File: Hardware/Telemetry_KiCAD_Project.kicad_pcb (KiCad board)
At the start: 4 copper layers, 80 x 93.3 mm, 68 parts, among them J1 TX SPI Debug, J2 RX SPI Debug, J3 Amphenol 132134 SMA Connector, J4 10118192-0001LF, J5 DB37_Male_MountingHoles, U1 Si4463, U2 ADL5521, U3 RSD-897.500-942.500-1612-TR, U4 LM317T, U5 USBLC6-2SC6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

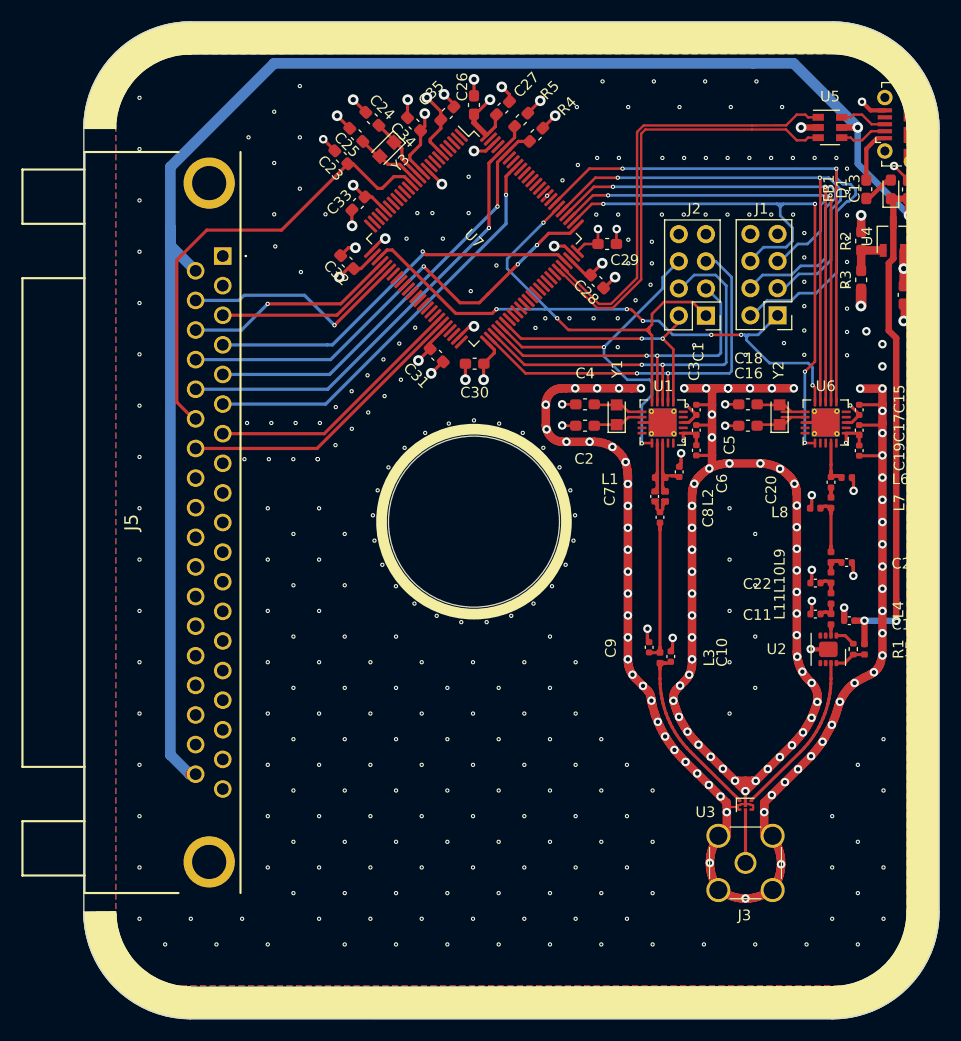
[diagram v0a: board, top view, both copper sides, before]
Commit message: Adjusted position of USB connector and components, length matched data lines
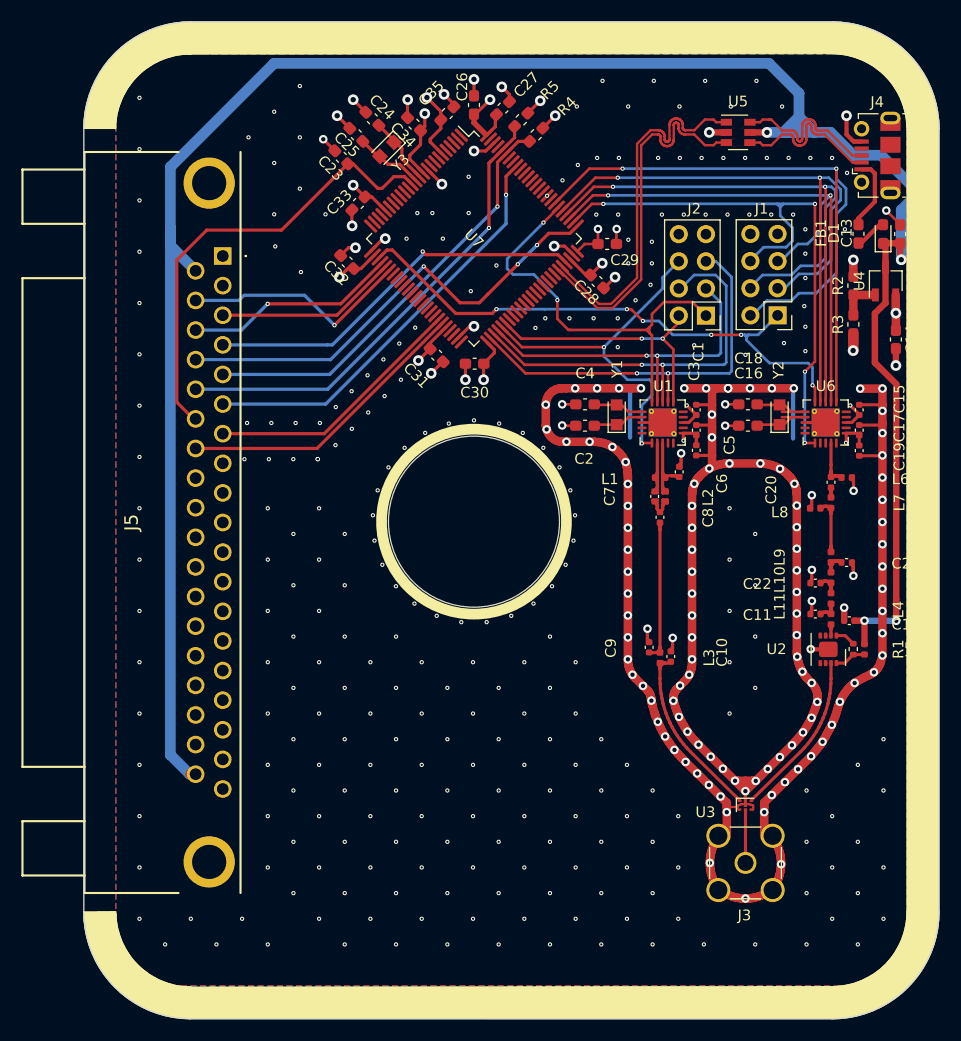
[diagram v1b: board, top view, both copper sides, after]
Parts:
- moved U5 8.60 mm to (141.2, 62.1)
- moved C14 4.23 mm to (156.0, 81.4)
- moved FB1 4.23 mm to (152.5, 71.5)
- moved C13 4.23 mm to (156.4, 71.6)
- moved D1 4.23 mm to (154.8, 71.6)
- moved R2 4.23 mm to (152.0, 76.4)
- moved R3 4.23 mm to (152.0, 80.0)
- moved U4 4.23 mm to (155.0, 76.0)
- moved J4 3.64 mm to (154.2, 64.2)
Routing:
- net +5V: track 195.6 -> 206.9 mm
- net /USB Connector and ESD/USB_CONN_D-: track 4.49 -> 15.0 mm
- net /USB Connector and ESD/USB_CONN_D+: track 4.51 -> 14.9 mm
- net GND: track 311.9 -> 322.1 mm, vias 418 -> 414
- net /USB Connector and ESD/D-: track 41.1 -> 35.0 mm
- net /USB Connector and ESD/D+: track 40.8 -> 34.7 mm
- net Net-(FB1-Pad2): track 5.07 -> 6.82 mm
- net /~RX_SEL: track 38.4 -> 39.6 mm

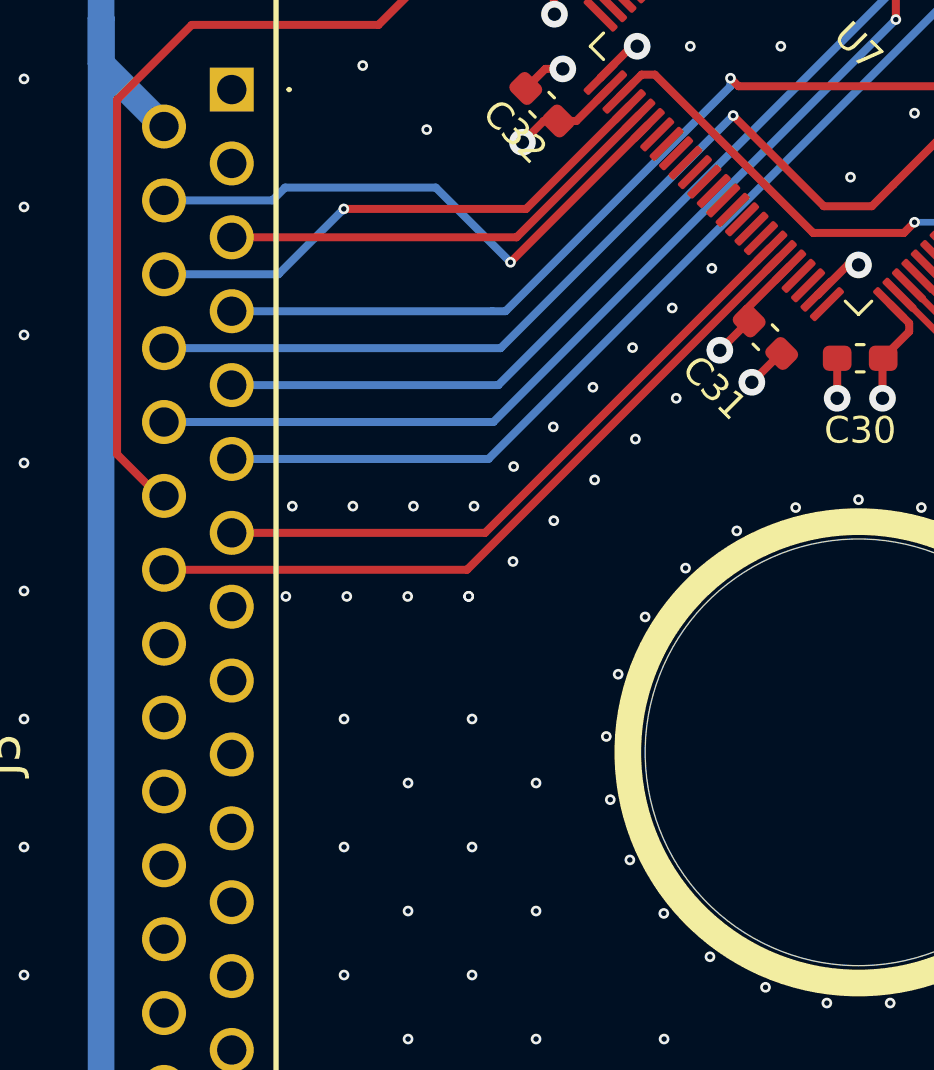
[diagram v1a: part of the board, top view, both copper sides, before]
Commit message: Added status LEDs for MCU
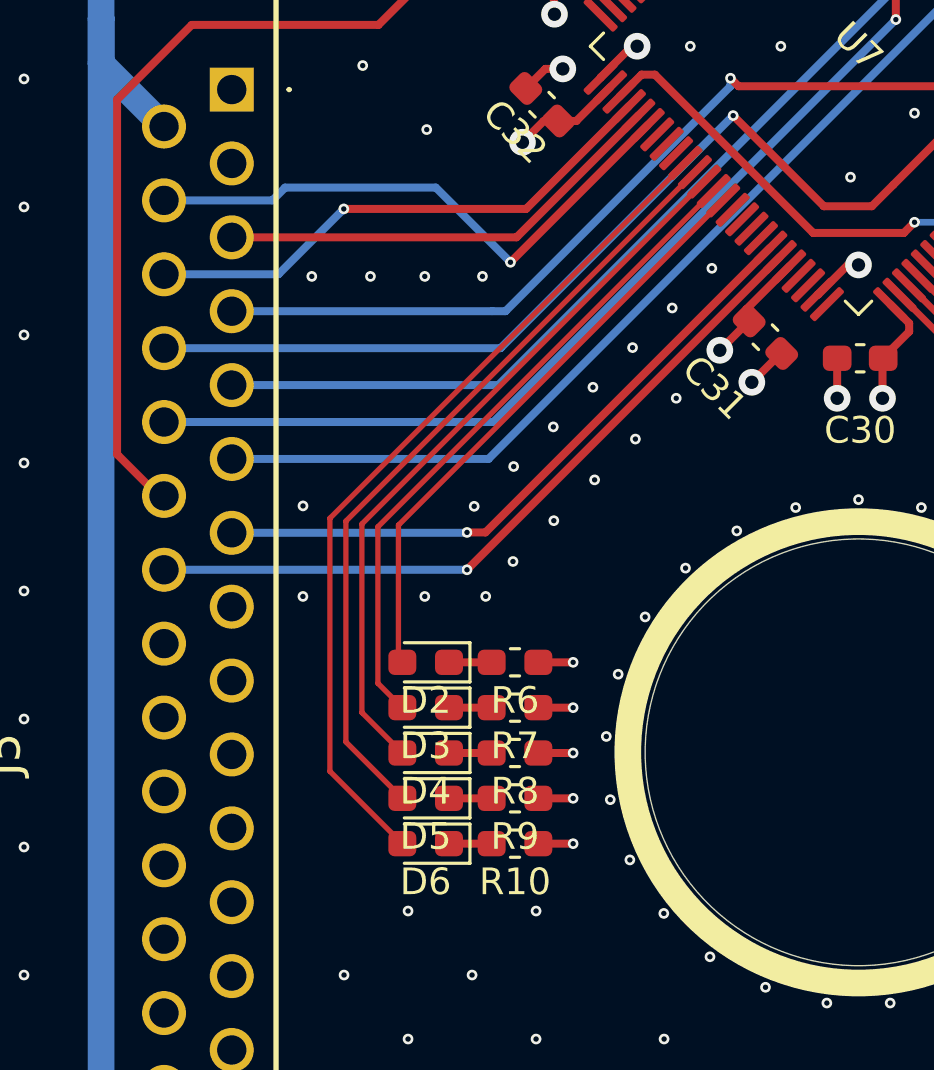
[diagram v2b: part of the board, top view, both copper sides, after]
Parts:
- added D2: Red, LED_SMD:LED_0603_1608Metric_Pad1.05x0.95mm_HandSolder, F.Cu at (100.3, 95.1)
- added D3: Grn, LED_SMD:LED_0603_1608Metric_Pad1.05x0.95mm_HandSolder, F.Cu at (100.3, 96.8)
- added D4: Red, LED_SMD:LED_0603_1608Metric_Pad1.05x0.95mm_HandSolder, F.Cu at (100.3, 98.5)
- added D5: Grn, LED_SMD:LED_0603_1608Metric_Pad1.05x0.95mm_HandSolder, F.Cu at (100.3, 100.2)
- added D6: Red, LED_SMD:LED_0603_1608Metric_Pad1.05x0.95mm_HandSolder, F.Cu at (100.3, 101.9)
- added R10: 820, Resistor_SMD:R_0603_1608Metric_Pad1.05x0.95mm_HandSolder, F.Cu at (103.6, 101.9)
- added R6: 820, Resistor_SMD:R_0603_1608Metric_Pad1.05x0.95mm_HandSolder, F.Cu at (103.6, 95.1)
- added R7: 820, Resistor_SMD:R_0603_1608Metric_Pad1.05x0.95mm_HandSolder, F.Cu at (103.6, 96.8)
- added R8: 820, Resistor_SMD:R_0603_1608Metric_Pad1.05x0.95mm_HandSolder, F.Cu at (103.6, 98.5)
- added R9: 820, Resistor_SMD:R_0603_1608Metric_Pad1.05x0.95mm_HandSolder, F.Cu at (103.6, 100.2)
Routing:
- net Net-(D6-Pad2): track 0.00 -> 32.2 mm
- net Net-(D5-Pad2): track 0.00 -> 29.8 mm
- net Net-(D4-Pad2): track 0.00 -> 27.4 mm
- net Net-(D3-Pad2): track 0.00 -> 25.0 mm
- net Net-(D2-Pad2): track 0.00 -> 22.4 mm
- net GND: track 322.1 -> 328.6 mm, vias 414 -> 413
- net Net-(D6-Pad1): track 0.00 -> 1.60 mm
- net Net-(D5-Pad1): track 0.00 -> 1.60 mm
- net Net-(D4-Pad1): track 0.00 -> 1.60 mm
- net Net-(D3-Pad1): track 0.00 -> 1.60 mm
- net Net-(D2-Pad1): track 0.00 -> 1.60 mm
- net /MCU_L562VE/ABORT_1: vias 0 -> 1
- net /MCU_L562VE/ABORT_2: vias 0 -> 1

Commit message: Added silk screen art
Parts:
- added G***: LOGO, Custom_Graphics:RDT_Logo, B.Cu at (102.7, 98.5)
- added G***: LOGO, Custom_Graphics:telemetry_qr_code, B.Cu at (121.8, 132.1)

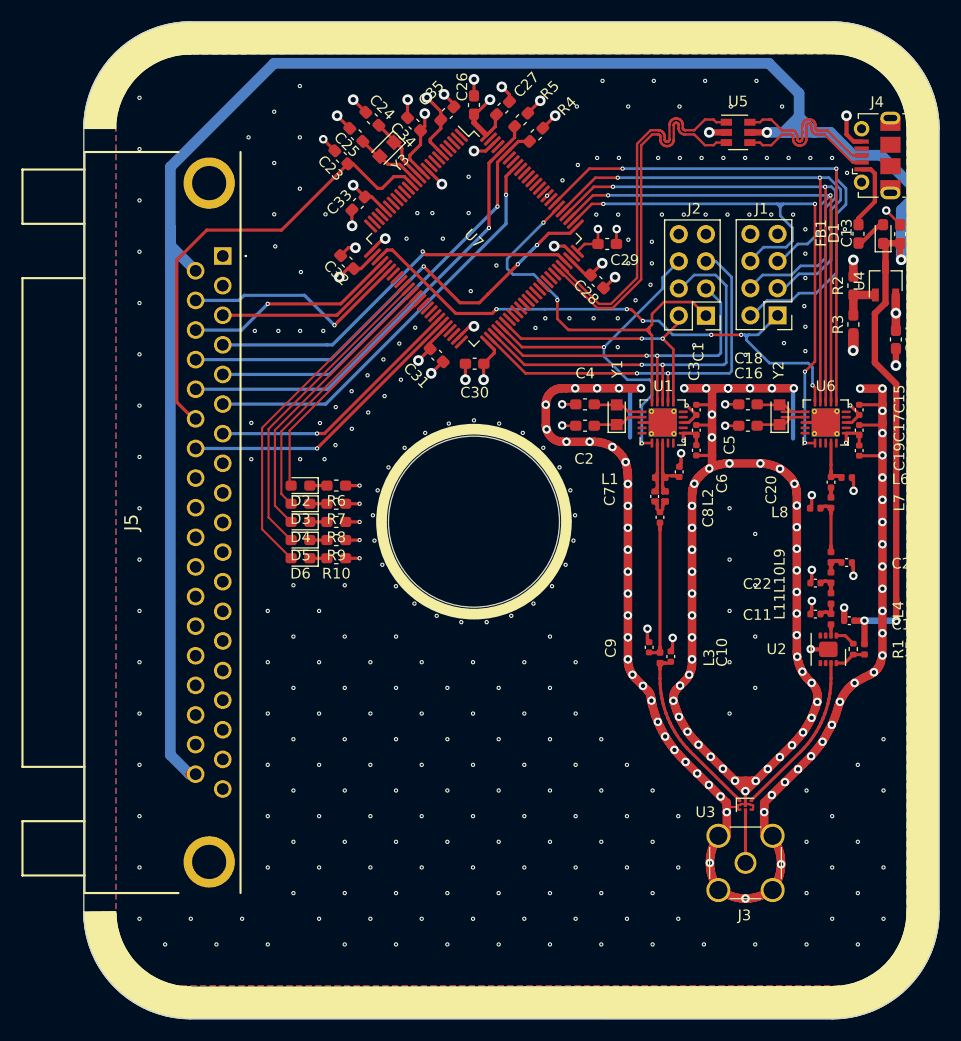
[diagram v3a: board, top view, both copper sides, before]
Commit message: Added larger crystals to TX/RX and MCU chips
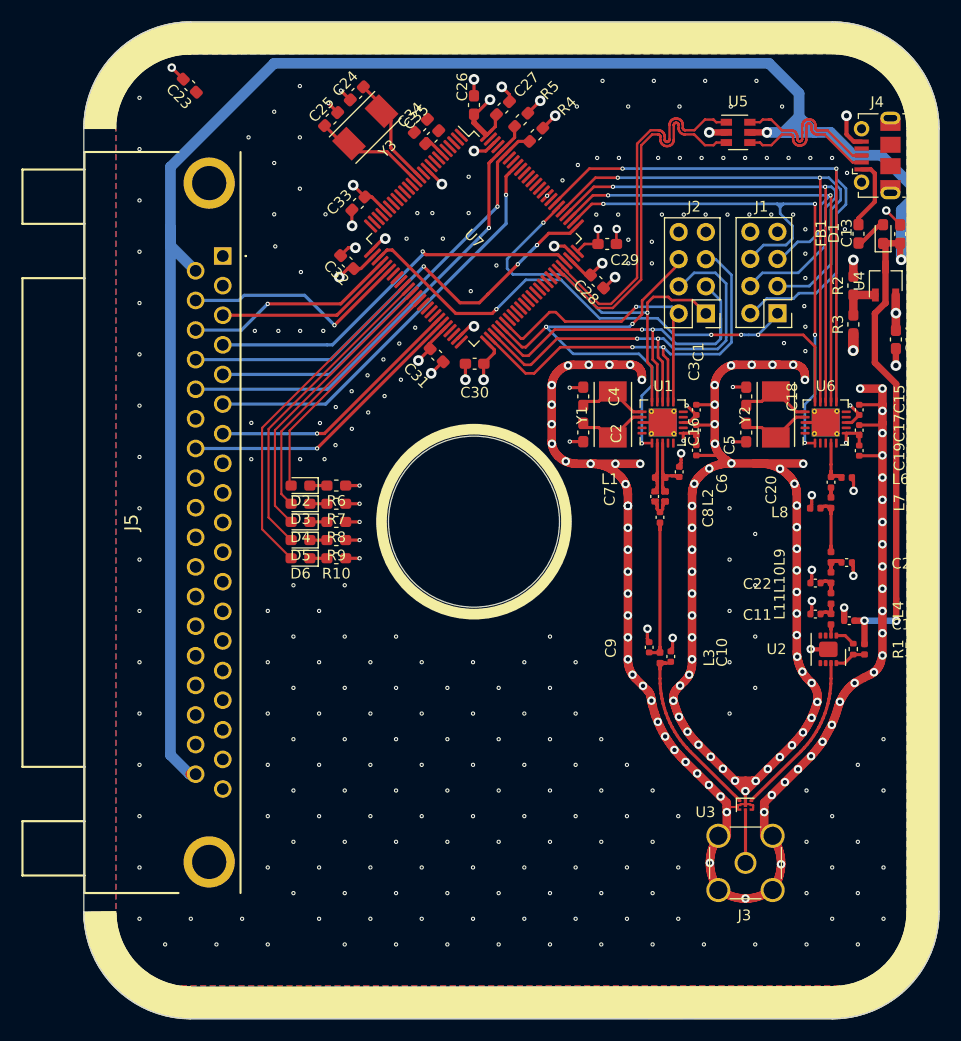
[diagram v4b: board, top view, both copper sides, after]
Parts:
- Y1, Y2, Y3: footprint Crystal:Crystal_SMD_2012-2Pin_2.0x1.2mm_HandSoldering -> RDT_Custom_Footprints:XTAL_ABM7-32.000MHZ-D2Y-T
- moved C23 15.7 mm to (89.9, 57.7)
- moved Y3 2.88 mm to (106.3, 61.6)
- moved C24 2.79 mm to (105.5, 58.4), turned to 225 degrees
- moved C25 2.78 mm to (103.1, 60.8), turned to 45 degrees
- moved C35 2.64 mm to (112.6, 62.5)
- moved C4 0.76 mm to (126.7, 86.8), turned to 90 degrees
- moved C18 0.76 mm to (142.0, 86.8), turned to 90 degrees
- moved C16 0.66 mm to (142.0, 90.1), turned to 270 degrees
- moved C34 0.66 mm to (111.5, 61.5), turned to 45 degrees
- moved C2 0.65 mm to (126.7, 90.1), turned to 270 degrees
- moved Y1 0.36 mm to (129.5, 88.4)
- moved Y2 0.35 mm to (144.7, 88.4)
- moved J1 0.20 mm to (144.9, 79.0)
- moved J2 0.20 mm to (138.2, 79.0)
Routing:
- net /37 Pin DSUB/NRST: track 43.2 -> 0.00 mm
- net +3V3: track 68.9 -> 58.0 mm, vias 18 -> 16
- net GND: track 328.6 -> 319.9 mm, vias 413 -> 380
- net /RX_RST: track 34.7 -> 41.7 mm, vias 2 -> 3
- net /RX_SDI: track 33.3 -> 38.3 mm
- net Net-(C24-Pad1): track 6.40 -> 10.6 mm
- net Net-(C25-Pad1): track 6.60 -> 10.7 mm
- net /~RX_IRQ: track 24.4 -> 28.1 mm, vias 2 -> 1
- net /RX_SDO: track 39.0 -> 41.4 mm
- net Net-(C4-Pad1): track 4.76 -> 7.09 mm
- net Net-(C2-Pad1): track 4.81 -> 7.08 mm
- net /~TX_SEL: track 53.5 -> 55.5 mm, vias 6 -> 4
- net /RX_SCL: track 38.5 -> 40.3 mm
- net Net-(C16-Pad1): track 5.71 -> 7.23 mm
- net Net-(C18-Pad1): track 5.66 -> 7.16 mm
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
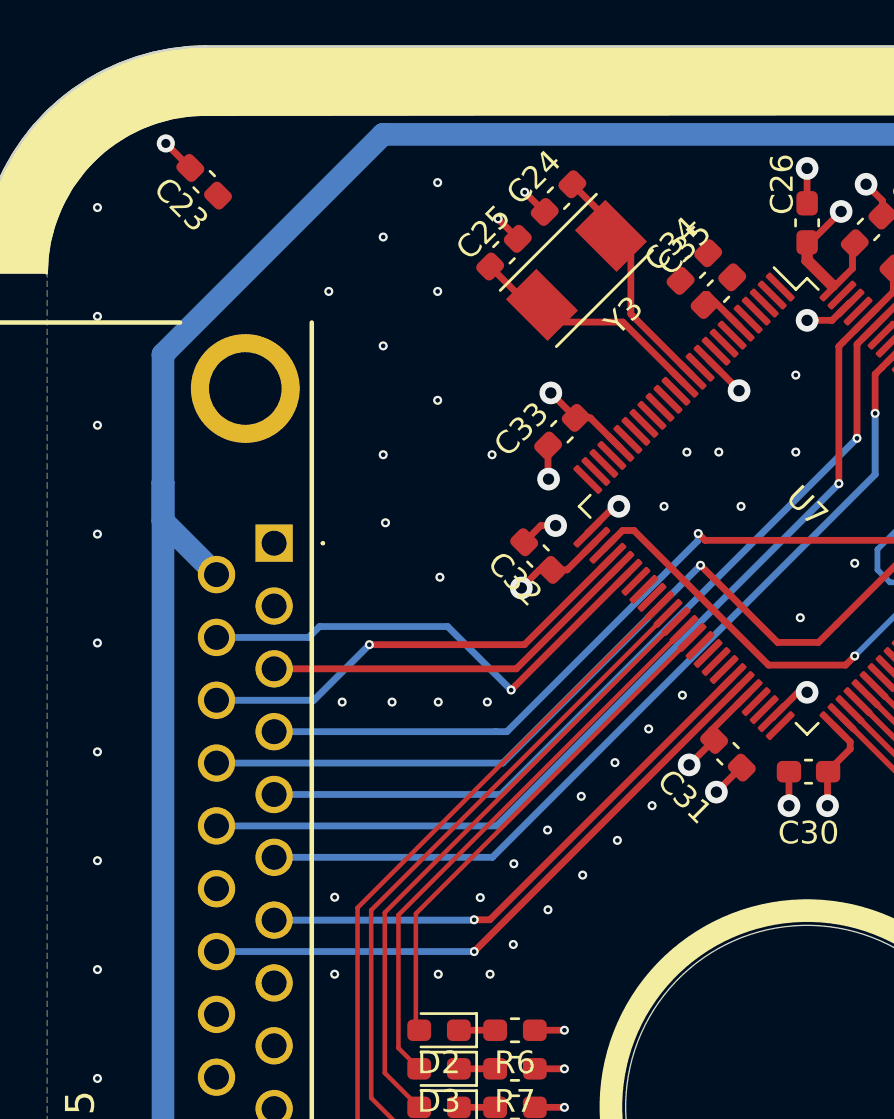
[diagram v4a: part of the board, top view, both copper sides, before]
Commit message: Added reset button to NRST line
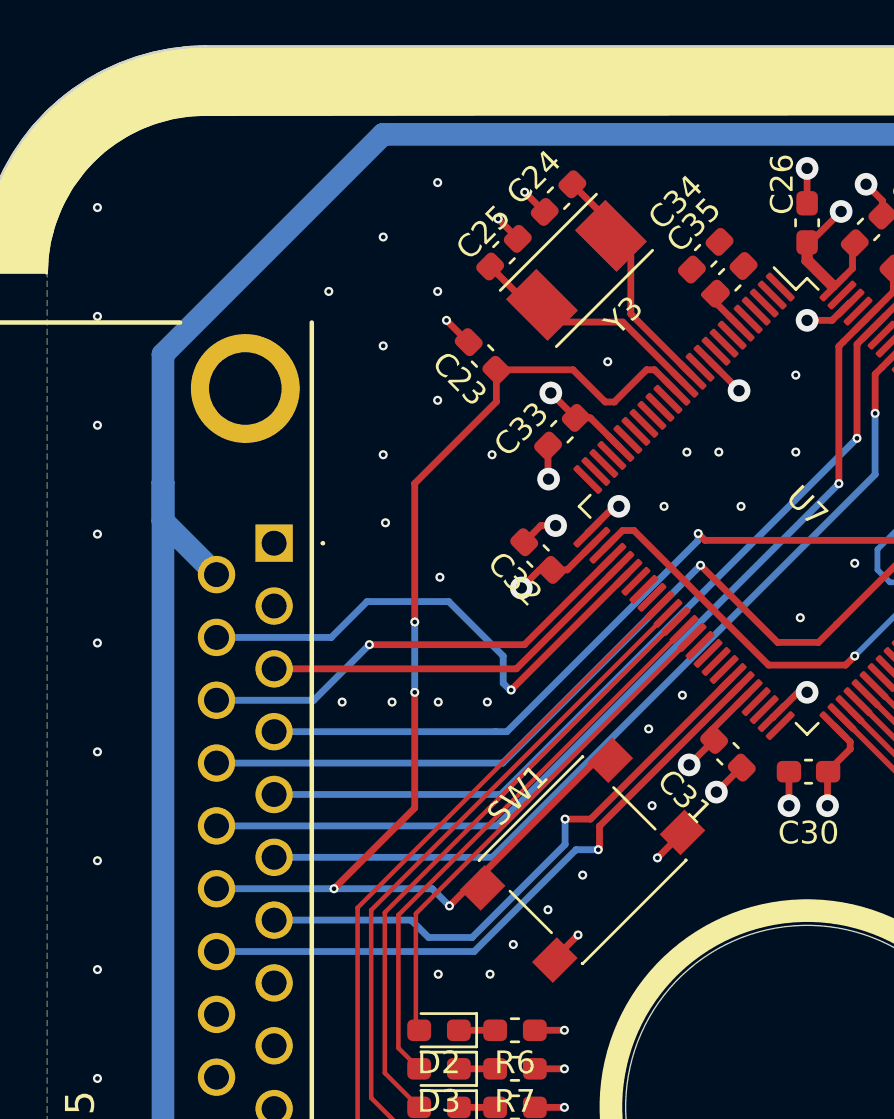
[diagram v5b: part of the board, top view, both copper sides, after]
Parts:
- added SW1: MCU Reset, Button_Switch_SMD:SW_SPST_PTS645, F.Cu at (106.6, 87.6)
- moved C23 14.5 mm to (102.2, 65.4)
- moved C34 0.71 mm to (112.0, 61.0)
- moved C35 0.71 mm to (113.1, 62.0)
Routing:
- net /37 Pin DSUB/NRST: track 0.00 -> 56.8 mm, vias 0 -> 4
- net GND: track 319.9 -> 322.9 mm, vias 380 -> 375
- net /MCU_L562VE/SPI1_MOSI: track 21.6 -> 23.2 mm
- net /MCU_L562VE/ABORT_1: track 24.6 -> 25.9 mm
- net /MCU_L562VE/ABORT_2: track 27.9 -> 28.5 mm
